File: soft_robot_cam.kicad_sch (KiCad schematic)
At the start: 82 parts, among them J1 Connector, J10 Screw_Terminal_01x02, J11 Conn_02x02_Counter_Clockwise, J2 Conn_01x06, J3 Conn_01x03, J4 Conn_01x05_Pin, J5 Conn_01x02_Pin, J6 Screw_Terminal_01x02, J7 Screw_Terminal_01x02, J8 Conn_01x24_Socket, J9 Screw_Terminal_01x02, Q1 S8050, Q2 S8050, Q3 AO3401A, Q4 AO3400A, SW3 SW_DP3T, SW4 SW_DIP_x02, SW5 SW_DP3T, U10 ICM-42605, U12 XC6206P282MR, U13 XC6206P122MR, U14 SY8113IADC, U3 MPU6500, U4 DRV8874PWPR, U5 DRV8874PWPR, U9 ESP32-S3-WROOM-1-N16R8

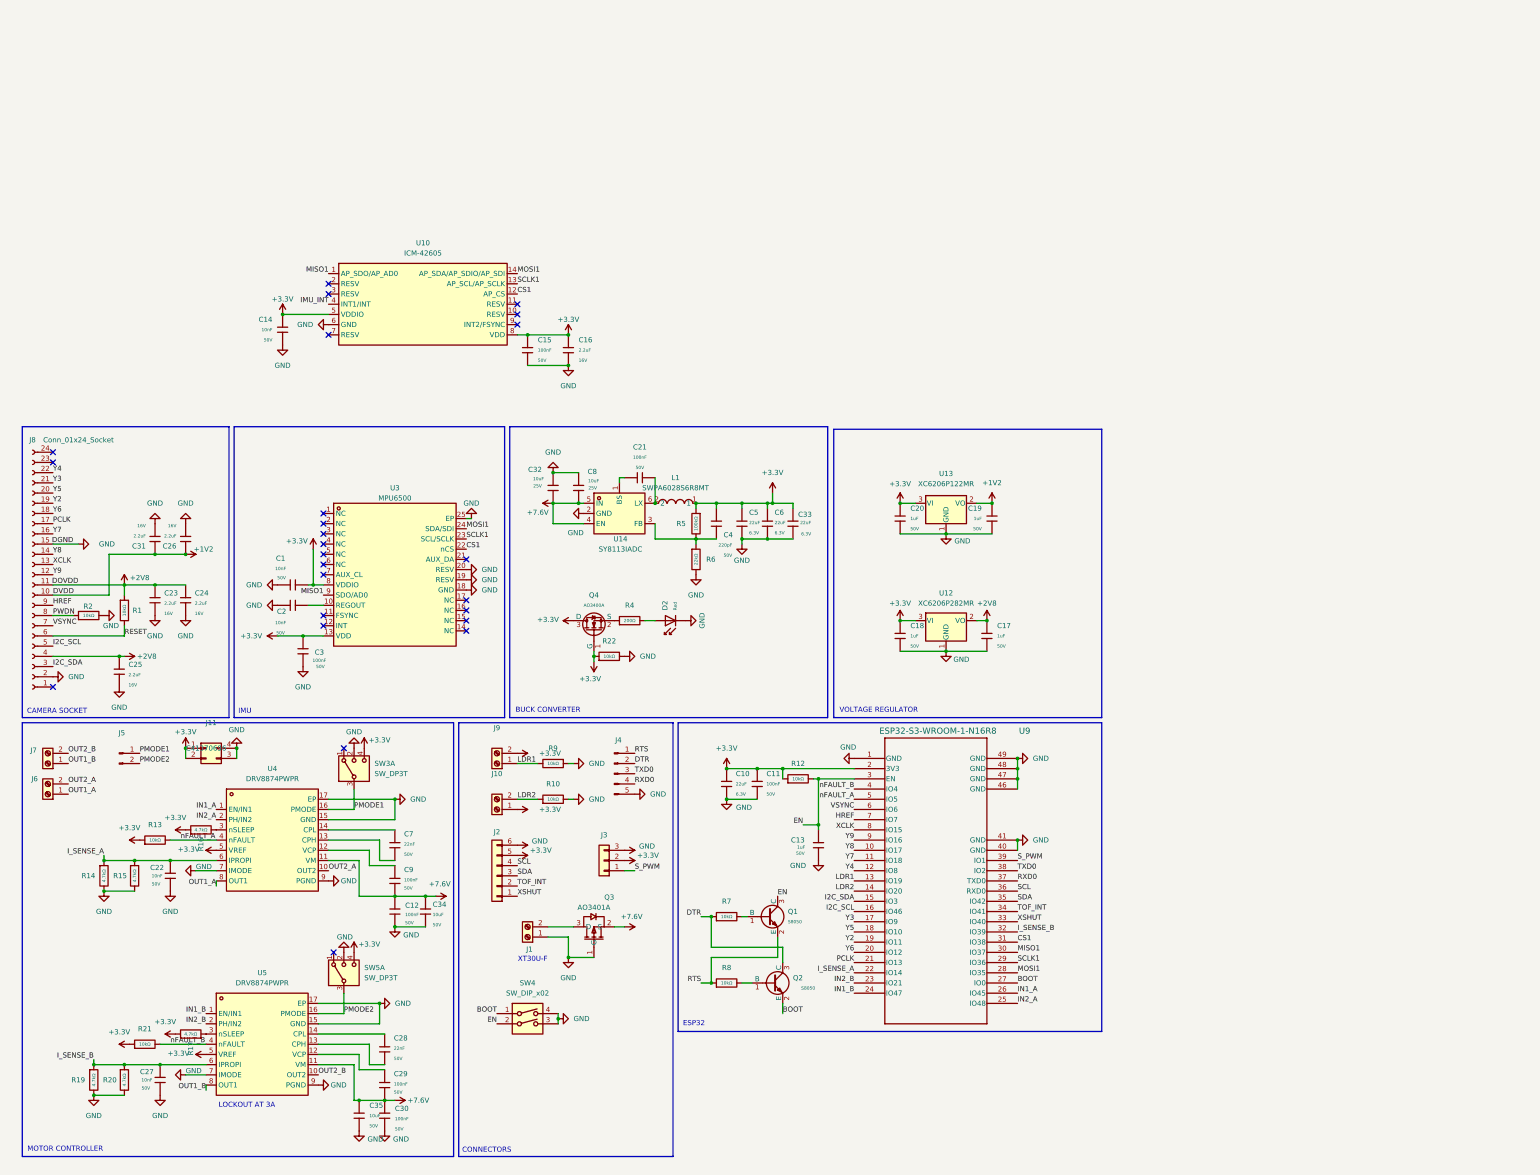
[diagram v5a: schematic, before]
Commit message: Reviewed and fixed wiring, adding eFuses and protection IC.
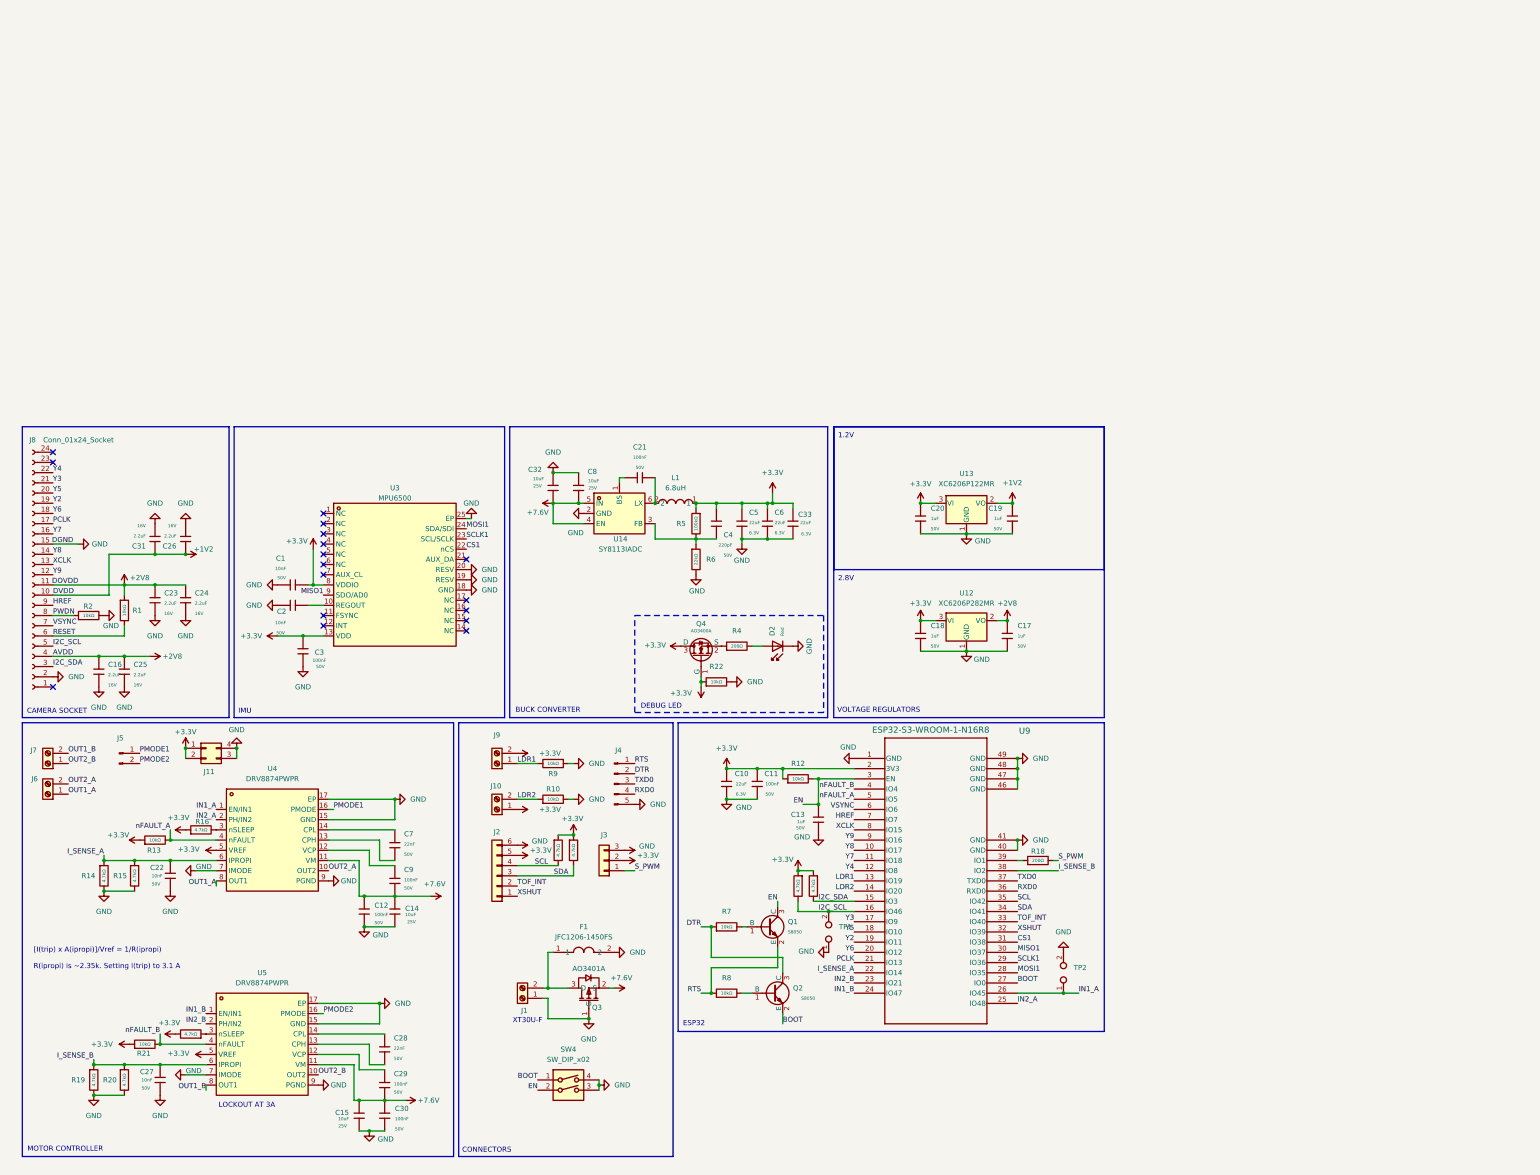
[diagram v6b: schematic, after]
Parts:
- removed C14: 10nF, PCM_JLCPCB:C_0603, symbol PCM_JLCPCB-Capacitors:0603,10nF
- removed C15: 100nF, PCM_JLCPCB:C_0603, symbol PCM_JLCPCB-Capacitors:0603,100nF
- removed C34, C35: 10uF, PCM_JLCPCB:C_1206, symbol PCM_JLCPCB-Capacitors:1206,10uF
- removed SW3, SW5: SW_DP3T, symbol Switch:SW_DP3T
- removed U10: ICM-42605, easyeda2kicad:LGA-14_L3.0-W2.5-P0.50-TL, symbol easyeda2kicad:ICM-42605
- added C14, C15: 10uF, PCM_JLCPCB:C_0603, symbol PCM_JLCPCB-Capacitors:0603,10uF,(2)
- added F1: JFC1206-1450FS, easyeda2kicad:F1206, symbol easyeda2kicad:JFC1206-1450FS
- added R11, R23, R24, R3: 4.7kΩ, PCM_JLCPCB:R_0603, symbol PCM_JLCPCB-Resistors:0603,4.7kΩ
- added R18: 200Ω, PCM_JLCPCB:R_0402, symbol PCM_JLCPCB-Resistors:0402,200Ω
- added TP1, TP2: TestPoint_2Pole, symbol Connector:TestPoint_2Pole
- L1: value SWPA6028S6R8MT -> 6.8uH; footprint easyeda2kicad:IND-SMD_L6.0-W6.0_SWPA6045S -> easyeda2kicad:IND-SMD_L6.0-W6.0_SRN6045; LCSC (none) -> C42370386; Name (none) -> SWPA6028S6R8MT
- Q3: LCSC (none) -> C15127
- U12: LCSC (none) -> C14255
- U13: LCSC (none) -> C2827649
- U14: LCSC (none) -> C479075; LCSC Part C479075 -> (none)
- U3: footprint easyeda2kicad:QFN40P300X300X95-25N -> Package_DFN_QFN:QFN-24-1EP_3x3mm_P0.4mm_EP1.75x1.6mm; LCSC (none) -> C50278; LCSC Part C50278 -> (none)
- U4, U5: LCSC (none) -> C1855818
- U9: LCSC (none) -> C2913202
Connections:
- net +2V8: now also C16.1
- net +3.3V: now also R11.1, R23.1, R24.1, R3.1; no longer C16.1
- net +7.6V: now also C14.1, C15.1
- net GND: now also C14.2, C15.2, F1.2, TP1.1, TP2.2
- net I2C_SCL: now also R24.2, TP1.2
- net I2C_SDA: now also R3.2
- net IN1_A: now also TP2.1
- net I_SENSE_B: now also U9.38 (IO2); no longer U9.32 (IO39)
- net OUT1_B: now also J7.2 (Pin_2); no longer J7.1 (Pin_1)
- net OUT2_B: now also J7.1 (Pin_1); no longer J7.2 (Pin_2)
- net RXD0: now also U9.36 (RXD0); no longer U9.37 (TXD0)
- net SCL: now also U9.35 (IO42), R11.2; no longer U9.36 (RXD0)
- net SDA: now also U9.34 (IO41), R23.2; no longer U9.35 (IO42)
- net S_PWM: now also R18.2; no longer U9.39 (IO1)
- net TOF_INT: now also U9.33 (IO40); no longer U9.34 (IO41)
- net TXD0: now also U9.37 (TXD0); no longer U9.38 (IO2)
- net XSHUT: now also U9.32 (IO39); no longer U9.33 (IO40)
- net at J1.2 (Pin_2), Q3.3 (D): now also F1.1
- new net: R18.1, U9.39 (IO1)
- no-connect marks 25 -> 17
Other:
- note added: "1.2V"
- note added: "2.8V"
- note added: "DEBUG LED"
- note added: "VOLTAGE REGULATORS"
- note added: "[I(trip) x A(ipropi)]/Vref = 1/R(ipropi) R(ipropi) is ~2.35k. Setting I(trip) to 3.1 A"
- note removed: "VOLTAGE REGULATOR"
- moved on the sheet: C12, C13, C17, C18, C19, C20, C25, D2, J1, J4, Q1, Q2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

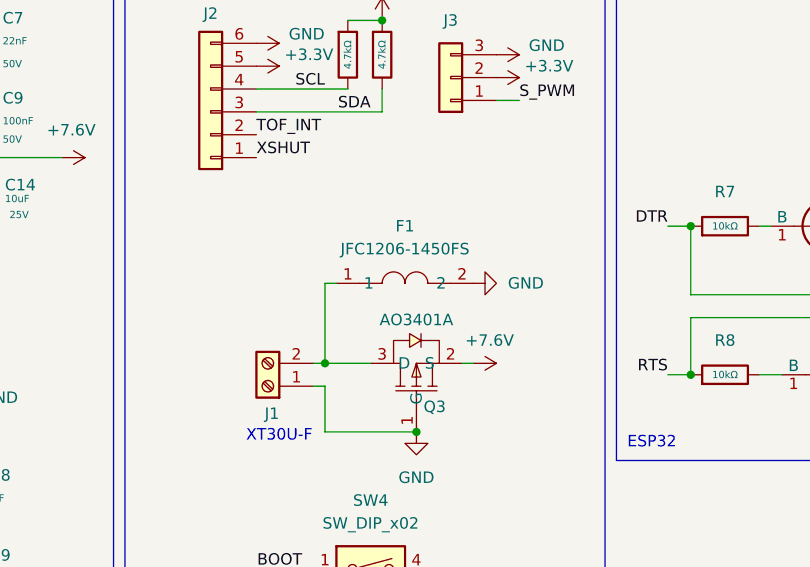
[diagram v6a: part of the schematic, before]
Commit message: Minor additions to PCB Layout, added branding and text
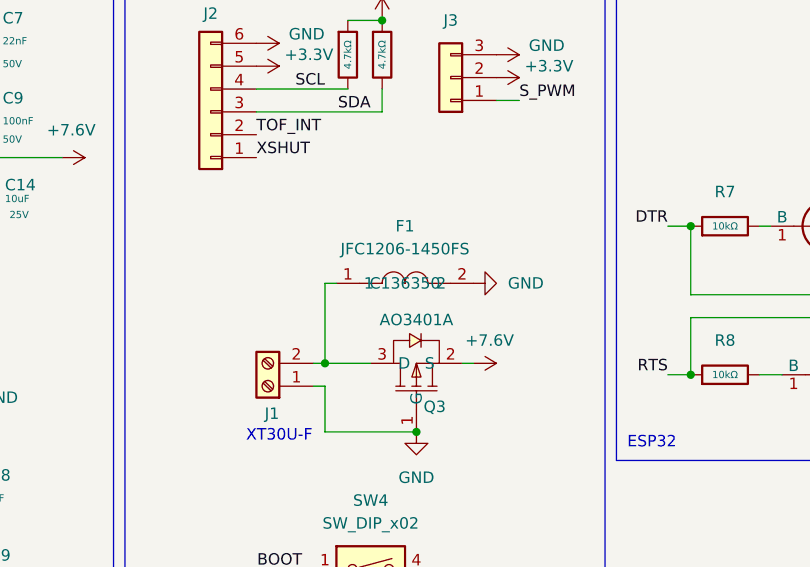
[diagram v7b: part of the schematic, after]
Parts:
- F1: LCSC (none) -> C136350
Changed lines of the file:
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@@
+			)
+		)
+		(property "LCSC" "C136350"
+			(at 153.67 144.78 0)
+			(effects
+				(font
+					(size 1.27 1.27)
+				)
 			)
 		)

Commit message: Minor Changes
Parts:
- added R25: 10kΩ, PCM_JLCPCB:R_0603, symbol PCM_JLCPCB-Resistors:0603,10kΩ
- added TP3: TestPoint_2Pole, symbol Connector:TestPoint_2Pole
- F1: LCSC C136350 -> (none); LCSC Part C136350 -> C41367230
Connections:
- net GND: now also R25.2, TP3.1
- net I2C_SDA: now also TP3.2
- net IN1_A: now also R25.1
